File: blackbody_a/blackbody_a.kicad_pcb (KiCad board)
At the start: 2 copper layers, 48.9 x 38.5 mm, 65 parts, among them IC1 LM76202QPWPRQ1, IC2 TPS562231DRLR, SW4 SW_SPDT, SW5 SW_Push, SW6 Reset, U1 LTC4311CSC6-TRPBF, U2 TCAN337DCNR, U3 STM32L431CBTx, Y1 8M

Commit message: layout edits
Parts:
- removed C11: 47uF, Capacitor_SMD:C_0805_2012Metric
- removed C14: 10uF, Capacitor_SMD:C_0805_2012Metric
- removed C15: 0.1uF, Capacitor_SMD:C_0805_2012Metric
- removed CarPower: CarPowerConnector, UTSVT_Connectors:Molex_MicroFit3.0_1x2xP3.00mm_PolarizingPeg_Vertical
- removed IC2: TPS562231DRLR, blackbody_a:TPS562231DRLR
- removed L1: 3.3uH, Inductor_SMD:L_0805_2012Metric
- removed R11: 45.3k, Resistor_SMD:R_0805_2012Metric
- removed R12: 10k, Resistor_SMD:R_0805_2012Metric
- removed R6: 200, Resistor_SMD:R_0805_2012Metric
- removed R7: 1k, Resistor_SMD:R_0805_2012Metric
- added C16: 10uF, Capacitor_SMD:C_0805_2012Metric, B.Cu at (148.1, 115.6)
- added C17: 0.1uF, Capacitor_SMD:C_0805_2012Metric, B.Cu at (147.9, 111.5)
- added C18: 10nF, Capacitor_SMD:C_0805_2012Metric, B.Cu at (153.7, 112.5)
- added C25: 4.7nF, Capacitor_SMD:C_0805_2012Metric, B.Cu at (154.5, 109.9)
- added C4: 33uF, Capacitor_SMD:C_0805_2012Metric, B.Cu at (152.0, 106.0)
- added D6: D, Diode_SMD:D_0805_2012Metric, B.Cu at (147.7, 106.0)
- added H1: MountingHole, MountingHole:MountingHole_3.2mm_M3, F.Cu at (117.8, 113.5)
- added H2: MountingHole, MountingHole:MountingHole_3.2mm_M3, F.Cu at (159.0, 84.4)
- added H3: MountingHole, MountingHole:MountingHole_3.2mm_M3, F.Cu at (159.2, 113.5)
- added H4: MountingHole, MountingHole:MountingHole_3.2mm_M3, F.Cu at (117.8, 84.4)
- added J1: CarPowerConnector, UTSVT_Connectors:Molex_MicroFit3.0_1x2xP3.00mm_PolarizingPeg_Vertical, F.Cu at (139.7, 83.4)
- added J2: Conn_02x04_Counter_Clockwise, Connector_PinHeader_2.54mm:PinHeader_2x04_P2.54mm_Vertical, F.Cu at (144.3, 105.0)
- added L2: 13.3uH, Inductor_SMD:L_0805_2012Metric, F.Cu at (149.9, 106.9)
- added Rosc1: 85.5k, Resistor_SMD:R_0805_2012Metric, B.Cu at (151.6, 115.6)
- added U4: TPS5403DR, blackbodies:D0008A_N, F.Cu at (149.9, 111.6)
- BlackbodyC1: footprint blackbodies:MOLEX_1053091104 -> Connector_Molex:Molex_Nano-Fit_105313-xx04_1x04_P2.50mm_Horizontal
- C10, C19, C2, C20, C21, C22, C3, C9, R18, R4, R8, R9: moved to B.Cu
- CAN_IN1, CAN_OUT1: footprint Connector_PinHeader_2.54mm:PinHeader_1x02_P2.54mm_Vertical -> blackbodies:CONN_SD-105309-100_02_MOL
- R1: moved to F.Cu
- R10: value 10K -> 20K; moved to B.Cu
- R5: value 10k -> 12k; moved to B.Cu
- moved CAN_OUT1 98.7 mm to (157.5, 93.3), turned to 90 degrees
- moved CAN_IN1 95.2 mm to (152.9, 85.3), turned to 180 degrees
- moved SWD1 87.8 mm to (144.0, 93.2), turned to 0 degrees
- moved R4 86.5 mm to (154.7, 101.0), turned to 0 degrees
- moved R18 85.5 mm to (154.6, 98.9), turned to 180 degrees
- moved JP1 83.9 mm to (154.7, 105.1), turned to 0 degrees
- moved TP1 83.3 mm to (161.1, 104.2)
- moved U2 81.5 mm to (154.8, 100.1)
- moved R8 80.9 mm to (153.7, 95.6), turned to 180 degrees
- moved TP4 79.0 mm to (161.1, 106.5)
- moved D1 78.1 mm to (148.7, 103.0)
- moved C23 77.4 mm to (141.8, 113.1)
- moved C3 75.6 mm to (144.3, 90.0)
- moved TP5 74.7 mm to (161.1, 108.8)
- moved SW5 73.5 mm to (138.9, 113.2)
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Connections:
- BlackbodyC1 pad 1: /SDA -> /SCL
- BlackbodyC1 pad 2: /SCL -> /SDA
- BlackbodyC1 pad 3: +3V3 -> +3.3V
- C1 pad 2: +3V3 -> +3.3V
- C19 pad 1: +3V3 -> +3.3V
- C20 pad 1: +3V3 -> +3.3V
- C21 pad 1: +3V3 -> +3.3V
- C22 pad 1: +3V3 -> +3.3V
- C9 pad 1: +3V3 -> +3.3V
- IC1 pad 13: /power_dist/RTN -> unconnected-(IC1-NC_2-Pad13)
- IC1 pad 4: /power_dist/RTN -> unconnected-(IC1-NC_1-Pad4)
- IC1 pad 6: /power_dist/RTN -> /power_dist/MODE
- R1 pad 1: +3V3 -> +3.3V
- R18 pad 1: +3V3 -> +3.3V
- R2 pad 1: +3V3 -> +3.3V
- R23 pad 1: +3V3 -> +3.3V
- R5 pad 1: /12V_Ext -> Net-(U4-COMP)
- R5 pad 2: /power_dist/UVLO -> Net-(C25-Pad2)
- SWD1 pad 1: +3V3 -> +3.3V
- U1 pad 1: +3V3 -> +3.3V
- U1 pad 3: +3V3 -> +3.3V
- U2 pad 2: +3V3 -> +3.3V
- U3 pad 15: unconnected-(U3-PA5-Pad15) -> /15
- U3 pad 16: unconnected-(U3-PA6-Pad16) -> /16
- U3 pad 17: unconnected-(U3-PA7-Pad17) -> /17
- U3 pad 18: unconnected-(U3-PB0-Pad18) -> /18
- U3 pad 19: unconnected-(U3-PB1-Pad19) -> /19
- U3 pad 20: unconnected-(U3-PB2-Pad20) -> /20
- U3 pad 21: unconnected-(U3-PB10-Pad21) -> /21
- U3 pad 22: unconnected-(U3-PB11-Pad22) -> /22
- U3 pad 24: +3V3 -> +3.3V
- U3 pad 36: +3V3 -> +3.3V
- U3 pad 48: +3V3 -> +3.3V
- U3 pad 9: +3V3 -> +3.3V
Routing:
- net +3V3: track 134.4 -> 0.00 mm, vias 9 -> 0
- net GND: track 103.9 -> 48.9 mm, vias 10 -> 17
- net /12V_Ext: track 54.9 -> 3.44 mm
- net +12V: track 55.5 -> 4.73 mm
- net /power_dist/RTN: track 55.1 -> 7.65 mm
- net /can_comm/Fault: track 39.6 -> 8.20 mm, vias 6 -> 1
- net /power_dist/OVP: track 30.3 -> 0.00 mm
- net /power_dist/UVLO: track 23.0 -> 0.00 mm
- net /SDA: track 31.1 -> 13.6 mm, vias 3 -> 1
- net Net-(IC1-DVDT): track 18.2 -> 1.27 mm, vias 2 -> 1
- net /SCL: track 36.0 -> 21.8 mm, vias 3 -> 1
- net /SWCLK: track 19.0 -> 5.48 mm, vias 2 -> 0
- net /I2C: track 27.0 -> 16.3 mm, vias 3 -> 1
- net /Error: track 25.8 -> 15.4 mm, vias 3 -> 1
- net /19: track 0.00 -> 10.3 mm, vias 0 -> 1
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- added copper zone on B.Cu, net (none)
- added copper zone on F.Cu, net (none)
- added copper zone on In1.Cu, net (none)
- added copper zone on In2.Cu, net (none)
- added copper zone on In1.Cu, net +12V
- added copper zone on F.Cu, net +3.3V
- added copper zone on In2.Cu, net /12V_Ext
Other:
- board size 48.9 x 38.5 mm -> 48.9 x 36.9 mm
- copper layers 2 -> 4

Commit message: layout updates
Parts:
- removed D11: I2C, LED_SMD:LED_0805_2012Metric
- removed D12: Heartbeat, LED_SMD:LED_0805_2012Metric
- removed D3: 12V, LED_SMD:LED_0805_2012Metric
- removed D4: 3.3V, LED_SMD:LED_0805_2012Metric
- removed D5: 12V_Ext, LED_SMD:LED_0805_2012Metric
- removed D8: Error, LED_SMD:LED_0805_2012Metric
- removed J2: Conn_02x04_Counter_Clockwise, Connector_PinHeader_2.54mm:PinHeader_2x04_P2.54mm_Vertical
- removed L2: 13.3uH, Inductor_SMD:L_0805_2012Metric
- removed SW4: SW_SPDT, Button_Switch_SMD:SW_DIP_SPSTx01_Slide_6.7x4.1mm_W6.73mm_P2.54mm_LowProfile_JPin
- removed TP1: 12V, TestPoint:TestPoint_Pad_D1.0mm
- removed TP4: 3V3, TestPoint:TestPoint_Pad_D1.0mm
- removed TP5: GND, TestPoint:TestPoint_Pad_D1.0mm
- added 12V: 12V, LED_SMD:LED_0805_2012Metric, F.Cu at (116.5, 89.9)
- added 12V: TestPoint, TestPoint:TestPoint_Pad_D1.0mm, F.Cu at (152.2, 115.7)
- added 12Vext: 12V, LED_SMD:LED_0805_2012Metric, F.Cu at (116.5, 92.1)
- added 3V3: TestPoint, TestPoint:TestPoint_Pad_D1.0mm, F.Cu at (147.2, 115.7)
- added 3V3: 3.3V, LED_SMD:LED_0805_2012Metric, F.Cu at (116.6, 94.3)
- added Error: Error, LED_SMD:LED_0805_2012Metric, F.Cu at (116.5, 101.2)
- added G***: LOGO, LOGO, B.Cu at (128.4, 86.5)
- added G***: LOGO, LOGO, B.Cu at (119.7, 105.9)
- added GND: TestPoint, TestPoint:TestPoint_Pad_D1.0mm, F.Cu at (142.2, 115.7)
- added Heartbeat: Heartbeat, LED_SMD:LED_0805_2012Metric, F.Cu at (116.6, 96.6)
- added I2C: I2C, LED_SMD:LED_0805_2012Metric, F.Cu at (116.6, 98.9)
- added J3: Conn_02x05_Counter_Clockwise, Connector_PinHeader_2.54mm:PinHeader_2x05_P2.54mm_Vertical, F.Cu at (139.0, 104.7)
- added L1: MSS1038-153MLC, blackbody_a:INDPM102100X400N, F.Cu at (147.1, 108.4)
- added Rosc2: 1k, Resistor_SMD:R_0805_2012Metric, B.Cu at (150.7, 109.0)
- added SW2: SW_DIP_x01, blackbodies:DS04254101BKSMT, F.Cu at (120.7, 106.0)
- C18: value 10nF -> 15nF
- C25: value 4.7nF -> 1nF
- C4: value 33uF -> 22uF
- D6: footprint Diode_SMD:D_0805_2012Metric -> blackbodies:SMA_DIO
- R18: value 2.2k -> 10k
- R5: value 12k -> 10k
- Rosc1: value 85.5k -> 84.5k
- moved H3 50.0 mm to (118.7, 84.2)
- moved H1 41.5 mm to (159.2, 113.7)
- moved H4 29.2 mm to (118.6, 113.7)
- moved C19 12.1 mm to (135.7, 101.4)
- moved C20 11.7 mm to (135.7, 99.4)
- moved C21 11.5 mm to (135.7, 97.4)
- moved C22 11.5 mm to (135.7, 95.4)
- moved D1 9.56 mm to (157.9, 100.7)
- moved C4 8.66 mm to (143.3, 105.7)
- moved U4 8.19 mm to (156.1, 106.3)
- moved R5 7.58 mm to (156.2, 104.5), turned to 90 degrees
- moved C17 7.39 mm to (153.2, 106.4), turned to 180 degrees
- moved Rosc1 7.14 mm to (154.2, 109.0), turned to 180 degrees
- moved C16 6.97 mm to (154.5, 113.0), turned to 90 degrees
- moved R21 6.90 mm to (117.4, 98.9)
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- renumbered BlackbodyC1 to BlackbodyC, D7 to CAN_Err, CAN_IN1 to CAN_IN, CAN_OUT1 to CAN_OUT, J1 to Power, SW6 to Reset, SWD1 to SWD
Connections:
- Rosc1 pad 2: GND -> Net-(Rosc1-Pad2)
- U3 pad 15: /15 -> unconnected-(U3-PA5-Pad15)
- U3 pad 16: /16 -> unconnected-(U3-PA6-Pad16)
- U3 pad 18: /18 -> unconnected-(U3-PB0-Pad18)
- U3 pad 19: /19 -> unconnected-(U3-PB1-Pad19)
- U3 pad 20: /20 -> unconnected-(U3-PB2-Pad20)
- U3 pad 21: /21 -> /UART_RX
- U3 pad 22: /22 -> /UART_TX
- U3 pad 25: unconnected-(U3-PB12-Pad25) -> /SPI_SS
- U3 pad 26: unconnected-(U3-PB13-Pad26) -> /SPI_SCK
- U3 pad 27: unconnected-(U3-PB14-Pad27) -> /SPI_MISO
- U3 pad 28: unconnected-(U3-PB15-Pad28) -> /SPI_MOSI
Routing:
- net +3.3V: track 33.3 -> 117.7 mm, vias 10 -> 13
- net /12V_Ext: track 3.44 -> 32.4 mm
- net +12V: track 4.73 -> 33.5 mm
- net /SCL: track 21.8 -> 41.1 mm, vias 1 -> 2
- net GND: track 48.9 -> 67.0 mm, vias 17 -> 11
- net /SDA: track 13.6 -> 30.2 mm
- net /SPI_MISO: track 0.00 -> 15.8 mm, vias 0 -> 1
- net /SPI_MOSI: track 0.00 -> 14.2 mm, vias 0 -> 1
- net /19: track 10.3 -> 0.00 mm, vias 1 -> 0
- net /21: track 10.3 -> 0.00 mm
- net /SPI_SCK: track 0.00 -> 10.1 mm, vias 0 -> 1
- net /SPI_SS: track 0.00 -> 7.71 mm, vias 0 -> 1
- net /22: track 7.67 -> 0.00 mm
- net /20: track 6.75 -> 0.00 mm
- net /15: track 6.54 -> 0.00 mm
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- added copper zone on F.Cu, net GND
- added copper zone on In1.Cu, net GND
- added copper zone on In2.Cu, net GND
- removed copper zone on B.Cu, net (none)
- removed copper zone on F.Cu, net (none)
- removed copper zone on In1.Cu, net (none)
- removed copper zone on In2.Cu, net (none)
- removed copper zone on F.Cu, net +3.3V
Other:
- board size 48.9 x 36.9 mm -> 48.3 x 37 mm
- board text added: "+ -"
- board text added: "BlackbodyA v1.0 Tanya Lertpradist Spring 2025"
- board text added: "HI LO"
- board text added: "MISO"
- board text added: "MOSI"
- board text added: "PA7"
- board text added: "RX"
- board text added: "SCK"
- board text added: "SCL"
- board text added: "SDA"
- board text added: "SS"
- board text added: "TX"

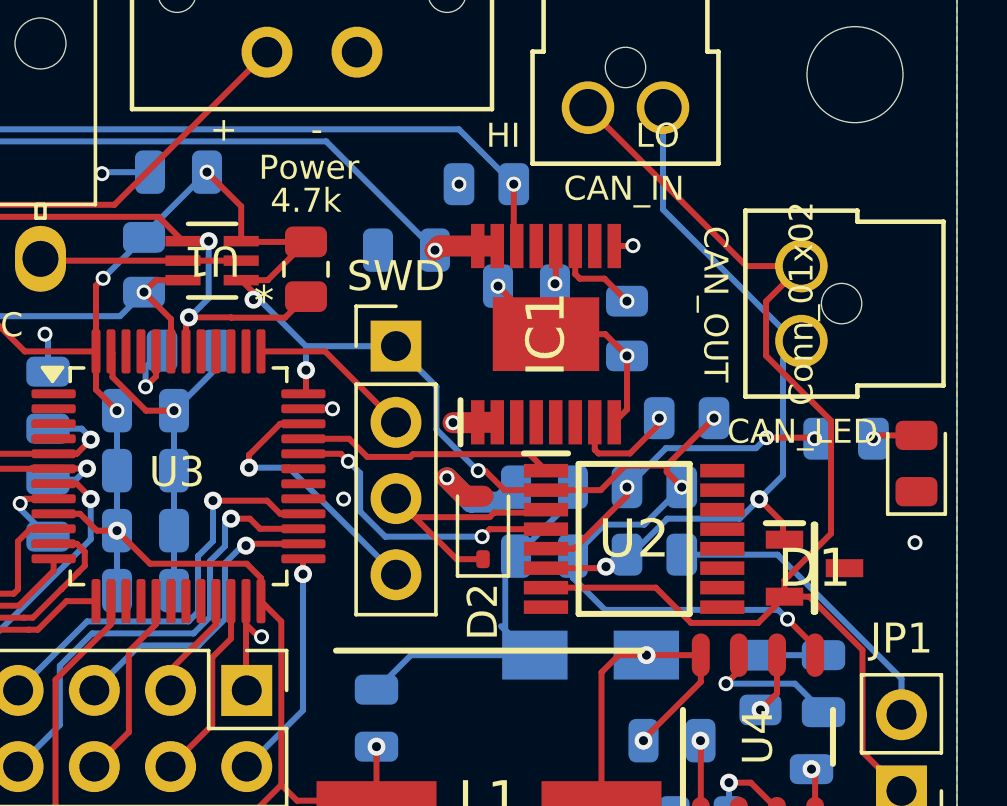
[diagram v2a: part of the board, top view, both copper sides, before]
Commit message: fixed footprint issue
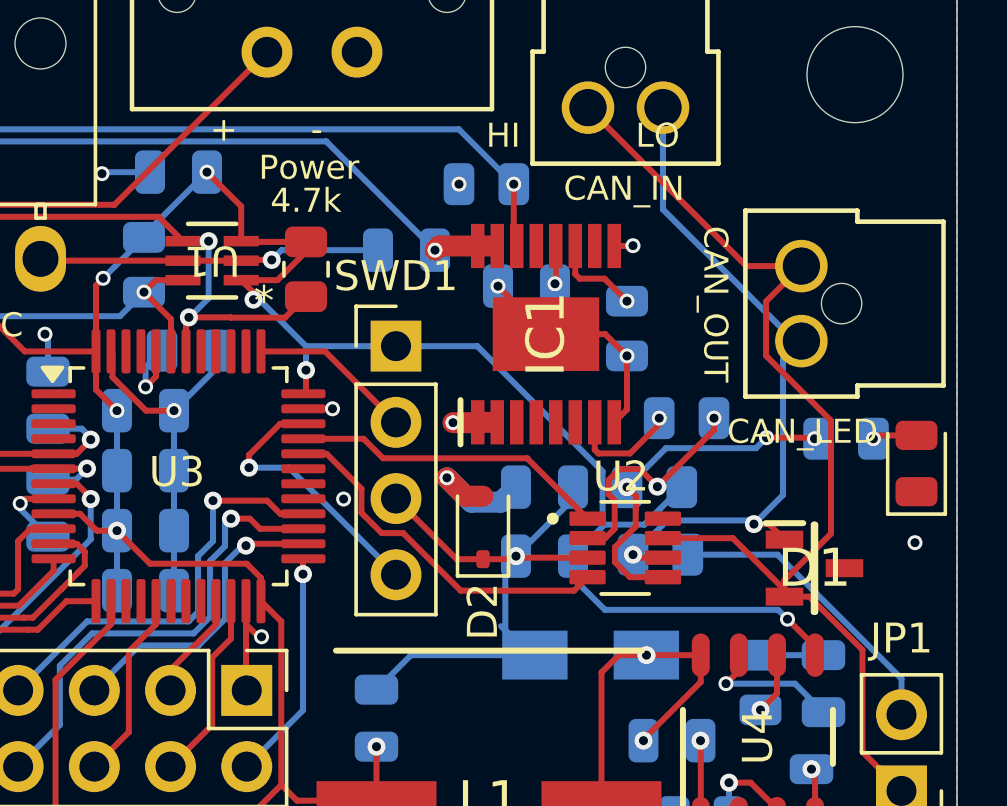
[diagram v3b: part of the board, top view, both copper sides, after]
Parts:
- U2: footprint UTSVT_ICs:SOP65P640X120-16N -> blackbody_a:SOT65P280X145-8N
- moved U2 0.42 mm to (151.6, 100.0)
- moved R4 0.20 mm to (152.8, 100.2)
- renumbered SWD to SWD1
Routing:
- net +3.3V: track 117.7 -> 121.6 mm, vias 13 -> 12
- net /CAN_H: track 39.7 -> 35.9 mm
- net GND: track 67.0 -> 70.2 mm, vias 11 -> 13
- net /CAN_L: track 26.1 -> 23.6 mm
- net /CAN_TX: track 8.60 -> 10.6 mm
- net /CAN_RX: track 10.1 -> 12.0 mm, vias 2 -> 0
- net /can_comm/Fault: track 10.7 -> 11.7 mm
